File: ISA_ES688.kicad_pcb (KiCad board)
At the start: 4 copper layers, 104.1 x 99.1 mm, 114 parts, among them J1 ISA BUS, J2 Interrupt Select, J3 Address Select, J4 DMA Select, J5 Joystick/MIDI, J6 LINE OUT, J7 MIC, J8 LINE IN, J9 SPKR OUT, U1 74LS14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

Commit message: Add OPL logo
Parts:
- added G***: LOGO, ES688_ISA8:opl_logo, F.Cu at (279.9, 140.5)
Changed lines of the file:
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@@
     (tracks 2242)
     (zones 0)
-    (modules 114)
+    (modules 115)
     (nets 141)
   )
@@
     (add_net GNDA)
   )
+  (module ES688_ISA8:opl_logo (layer F.Cu)
+    (at 279.908 140.462)
+    (fp_text reference G*** (at 0 0) (layer F.SilkS) hide
+      (effects (font (size 1.524 1.524) (thickness 0.3)))
+    )
+    (fp_text value LOGO (at 0.75 0) (layer F.SilkS) hide
+      (effects (font (size 1.524 1.524) (thickness 0.3)))
+    )
+    (fp_poly (pts (xy -5.344685 -3.755461) (xy -5.028291 -3.532553) (xy -4.870695 -3.306566) (xy -4.785234 -3.06096)
+      (xy -4.836403 -2.880506) (xy -5.038005 -2.734348) (xy -5.148945 -2.684645) (xy -5.340285 -2.602747)
+      (xy -5.385019 -2.564591) (xy -5.293745 -2.550992) (xy -5.224318 -2.548228) (xy -4.929154 -2.46042)
+      (xy -4.69366 -2.238158) (xy -4.530761 -1.909744) (xy -4.453385 -1.503478) (xy -4.474458 -1.047663)
+      (xy -4.492892 -0.946891) (xy -4.735392 -0.17358) (xy -5.125128 0.575267) (xy -5.640015 1.277122)
+      (xy -6.257967 1.909459) (xy -6.9569 2.449749) (xy -7.714727 2.875466) (xy -8.509363 3.16408)
+      (xy -8.527992 3.168951) (xy -8.915534 3.257863) (xy -9.212041 3.28867) (xy -9.485398 3.261724)
+      (xy -9.803493 3.177379) (xy -9.809211 3.175598) (xy -10.27074 2.946837) (xy -10.64008 2.586699)
+      (xy -10.904681 2.113241) (xy -10.991105 1.779589) (xy -9.986381 1.779589) (xy -9.931695 2.127449)
+      (xy -9.858866 2.267161) (xy -9.660316 2.419537) (xy -9.361963 2.447399) (xy -8.959009 2.350373)
+      (xy -8.517884 2.16324) (xy -7.777485 1.721081) (xy -7.078147 1.145927) (xy -6.456397 0.474058)
+      (xy -5.948764 -0.258248) (xy -5.795526 -0.540542) (xy -5.625997 -0.935733) (xy -5.523953 -1.295382)
+      (xy -5.492475 -1.590942) (xy -5.534641 -1.793864) (xy -5.6515 -1.875435) (xy -6.136229 -1.846969)
+      (xy -6.695017 -1.693987) (xy -7.301904 -1.428612) (xy -7.930931 -1.062966) (xy -8.556139 -0.609172)
+      (xy -8.79995 -0.405155) (xy -9.194592 -0.002926) (xy -9.521744 0.444896) (xy -9.770218 0.910078)
+      (xy -9.928826 1.364387) (xy -9.986381 1.779589) (xy -10.991105 1.779589) (xy -11.051994 1.544523)
+      (xy -11.071343 1.359395) (xy -11.037587 0.657076) (xy -10.837736 -0.038683) (xy -10.475021 -0.72296)
+      (xy -9.952673 -1.390831) (xy -9.273923 -2.037374) (xy -8.442001 -2.657664) (xy -8.429934 -2.665705)
+      (xy -7.982337 -2.940247) (xy -7.490359 -3.203266) (xy -6.989666 -3.439293) (xy -6.515922 -3.632857)
+      (xy -6.104792 -3.768486) (xy -5.791941 -3.83071) (xy -5.738926 -3.833013) (xy -5.344685 -3.755461)) (layer F.SilkS) (width 0.01))
+    (fp_poly (pts (xy 0.503216 -3.833673) (xy 1.041462 -3.79121) (xy 1.478677 -3.711661) (xy 1.848138 -3.588639)
+      (xy 2.183117 -3.415761) (xy 2.233753 -3.384306) (xy 2.532571 -3.162193) (xy 2.733427 -2.918503)
+      (xy 2.853094 -2.61487) (xy 2.908349 -2.212928) (xy 2.917597 -1.820333) (xy 2.907511 -1.412893)
+      (xy 2.875215 -1.120056) (xy 2.811183 -0.887569) (xy 2.718102 -0.684242) (xy 2.362164 -0.171137)
+      (xy 1.871179 0.295316) (xy 1.277327 0.6951) (xy 0.612788 1.008196) (xy -0.090259 1.214587)
+      (xy -0.421112 1.26859) (xy -0.871948 1.311872) (xy -1.370258 1.343292) (xy -1.80978 1.356183)
+      (xy -1.818112 1.356208) (xy -2.497667 1.35775) (xy -2.921 2.084592) (xy -3.259968 2.611556)
+      (xy -3.568713 2.977675) (xy -3.845679 3.181926) (xy -4.089313 3.223283) (xy -4.29806 3.100724)
+      (xy -4.355533 3.029161) (xy -4.449987 2.854031) (xy -4.472924 2.670727) (xy -4.417048 2.445085)
+      (xy -4.275062 2.142937) (xy -4.099923 1.832313) (xy -3.91802 1.514983) (xy -3.814334 1.307527)
+      (xy -3.778129 1.175737) (xy -3.798667 1.0854) (xy -3.845923 1.023083) (xy -3.937024 0.839818)
+      (xy -3.979014 0.592448) (xy -3.979333 0.570978) (xy -3.904121 0.265069) (xy -3.79781 0.156237)
+      (xy -1.719497 0.156237) (xy -1.612922 0.238973) (xy -1.370759 0.290498) (xy -1.024672 0.306059)
+      (xy -0.785444 0.296504) (xy -0.280216 0.212722) (xy 0.278712 0.035556) (xy 0.387038 -0.007965)
+      (xy 1.005987 -0.306772) (xy 1.482386 -0.63448) (xy 1.842784 -1.011098) (xy 1.976732 -1.205965)
+      (xy 2.143766 -1.539879) (xy 2.17021 -1.79664) (xy 2.050468 -2.001327) (xy 1.778941 -2.179017)
+      (xy 1.757155 -2.18963) (xy 1.333872 -2.356314) (xy 0.89357 -2.468623) (xy 0.496218 -2.514)
+      (xy 0.277307 -2.49951) (xy 0.168494 -2.465977) (xy 0.057079 -2.394658) (xy -0.073779 -2.266019)
+      (xy -0.240923 -2.060526) (xy -0.461193 -1.758646) (xy -0.751432 -1.340845) (xy -0.865693 -1.173828)
+      (xy -1.141812 -0.765139) (xy -1.380016 -0.404645) (xy -1.5655 -0.115412) (xy -1.683456 0.079497)
+      (xy -1.719497 0.156237) (xy -3.79781 0.156237) (xy -3.682503 0.038197) (xy -3.320511 -0.104335)
+      (xy -3.181404 -0.130465) (xy -3.043805 -0.155523) (xy -2.928346 -0.198082) (xy -2.815014 -0.279107)
+      (xy -2.683794 -0.419561) (xy -2.51467 -0.640409) (xy -2.287629 -0.962614) (xy -2.033471 -1.33284)
+      (xy -1.248217 -2.480827) (xy -1.745942 -2.434846) (xy -2.116111 -2.376256) (xy -2.52533 -2.275935)
+      (xy -2.751667 -2.203094) (xy -3.070246 -2.095598) (xy -3.368429 -2.009851) (xy -3.534833 -1.973065)
+      (xy -3.725644 -1.958874) (xy -3.800654 -2.013857) (xy -3.809186 -2.086237) (xy -3.758052 -2.226327)
+      (xy -3.625226 -2.453409) (xy -3.440283 -2.726831) (xy -3.232801 -3.005941) (xy -3.032354 -3.250087)
+      (xy -2.868521 -3.418615) (xy -2.807637 -3.46286) (xy -2.491422 -3.58177) (xy -2.04196 -3.684618)
+      (xy -1.494987 -3.766221) (xy -0.88624 -3.821397) (xy -0.251456 -3.844964) (xy -0.169333 -3.845435)
+      (xy 0.503216 -3.833673)) (layer F.SilkS) (width 0.01))
+    (fp_poly (pts (xy 6.792524 -3.750129) (xy 6.968282 -3.621872) (xy 7.027333 -3.453164) (xy 6.982386 -3.323082)
+      (xy 6.858223 -3.081252) (xy 6.670866 -2.755941) (xy 6.436334 -2.375415) (xy 6.273265 -2.122643)
+      (xy 5.937648 -1.604888) (xy 5.558663 -1.010002) (xy 5.179524 -0.406375) (xy 4.843445 0.137599)
+      (xy 4.798297 0.211667) (xy 4.077398 1.397) (xy 4.430532 1.453363) (xy 4.671015 1.487661)
+      (xy 5.021594 1.532665) (xy 5.423994 1.581027) (xy 5.630333 1.604612) (xy 6.233483 1.684084)
+      (xy 6.758622 1.776651) (xy 7.185292 1.877139) (xy 7.493035 1.980378) (xy 7.661392 2.081196)
+      (xy 7.686221 2.124361) (xy 7.644179 2.248616) (xy 7.509438 2.449922) (xy 7.310177 2.686746)
+      (xy 7.289679 2.70877) (xy 6.867463 3.158486) (xy 6.164232 3.102333) (xy 5.722562 3.063039)
+      (xy 5.241381 3.014062) (xy 4.826 2.966141) (xy 4.190005 2.905187) (xy 3.550565 2.878429)
+      (xy 2.944805 2.884863) (xy 2.409851 2.923485) (xy 1.98283 2.99329) (xy 1.798258 3.048043)
+      (xy 1.457049 3.166205) (xy 1.23689 3.208893) (xy 1.10809 3.17777) (xy 1.046545 3.090144)
+      (xy 1.029114 2.871373) (xy 1.131844 2.593413) (xy 1.362268 2.237436) (xy 1.416402 2.165557)
+      (xy 1.673378 1.876669) (xy 1.936897 1.696224) (xy 2.139321 1.614499) (xy 2.247521 1.576507)
+      (xy 2.344585 1.531112) (xy 2.441818 1.463876) (xy 2.550531 1.360364) (xy 2.682031 1.206141)
+      (xy 2.847627 0.98677) (xy 3.058627 0.687817) (xy 3.32634 0.294844) (xy 3.662073 -0.206584)
+      (xy 4.077134 -0.830903) (xy 4.200495 -1.016725) (xy 4.592092 -1.603086) (xy 4.961021 -2.148745)
+      (xy 5.295287 -2.636475) (xy 5.582899 -3.049049) (xy 5.811863 -3.369238) (xy 5.970187 -3.579815)
+      (xy 6.040507 -3.659951) (xy 6.280583 -3.779238) (xy 6.547273 -3.805941) (xy 6.792524 -3.750129)) (layer F.SilkS) (width 0.01))
+    (fp_poly (pts (xy 9.153934 -3.630036) (xy 9.394952 -3.60197) (xy 9.519474 -3.562208) (xy 9.525 -3.556)
+      (xy 9.48923 -3.498388) (xy 9.316743 -3.471958) (xy 9.275997 -3.471333) (xy 8.974667 -3.471333)
+      (xy 8.974667 -2.751667) (xy 8.969244 -2.391872) (xy 8.949508 -2.171664) (xy 8.91025 -2.061543)
+      (xy 8.847667 -2.032) (xy 8.784173 -2.062725) (xy 8.745313 -2.174567) (xy 8.72588 -2.397027)
+      (xy 8.720667 -2.751667) (xy 8.720667 -3.471333) (xy 8.466667 -3.471333) (xy 8.288325 -3.495858)
+      (xy 8.212686 -3.554947) (xy 8.212667 -3.556) (xy 8.291405 -3.59875) (xy 8.504313 -3.628518)
+      (xy 8.816428 -3.640604) (xy 8.84267 -3.640667) (xy 9.153934 -3.630036)) (layer F.SilkS) (width 0.01))
+    (fp_poly (pts (xy 9.927514 -3.58917) (xy 10.04666 -3.418926) (xy 10.181623 -3.118589) (xy 10.390503 -2.596511)
+      (xy 10.55705 -3.097422) (xy 10.670946 -3.395463) (xy 10.777338 -3.559898) (xy 10.898221 -3.623865)
+      (xy 10.907465 -3.625389) (xy 10.992412 -3.629646) (xy 11.046124 -3.591831) (xy 11.075746 -3.481508)
+      (xy 11.088424 -3.268238) (xy 11.091304 -2.921587) (xy 11.091333 -2.842222) (xy 11.086839 -2.457202)
+      (xy 11.0704 -2.213038) (xy 11.037577 -2.081418) (xy 10.983932 -2.03403) (xy 10.964333 -2.032)
+      (xy 10.893792 -2.06865) (xy 10.853097 -2.1993) (xy 10.835091 -2.455007) (xy 10.832603 -2.6035)
+      (xy 10.827872 -3.175) (xy 10.673454 -2.794) (xy 10.52987 -2.521995) (xy 10.387411 -2.414657)
+      (xy 10.36774 -2.413) (xy 10.2341 -2.489213) (xy 10.108379 -2.723857) (xy 10.082389 -2.794)
+      (xy 9.948333 -3.175) (xy 9.923298 -2.6035) (xy 9.899523 -2.281268) (xy 9.858687 -2.100609)
+      (xy 9.793667 -2.034057) (xy 9.775131 -2.032) (xy 9.716092 -2.063684) (xy 9.678723 -2.177111)
+      (xy 9.658807 -2.399846) (xy 9.652124 -2.759452) (xy 9.652 -2.836333) (xy 9.654859 -3.21099)
+      (xy 9.667581 -3.447542) (xy 9.696385 -3.577178) (xy 9.747491 -3.631087) (xy 9.812371 -3.640667)
+      (xy 9.927514 -3.58917)) (layer F.SilkS) (width 0.01))
+  )
   (module ES688_ISA8:SOP-16 (layer F.Cu)

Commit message: Change silkscreen
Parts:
- moved G*** 2.36 mm to (281.3, 142.4)
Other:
- board text added: "INSIDE"

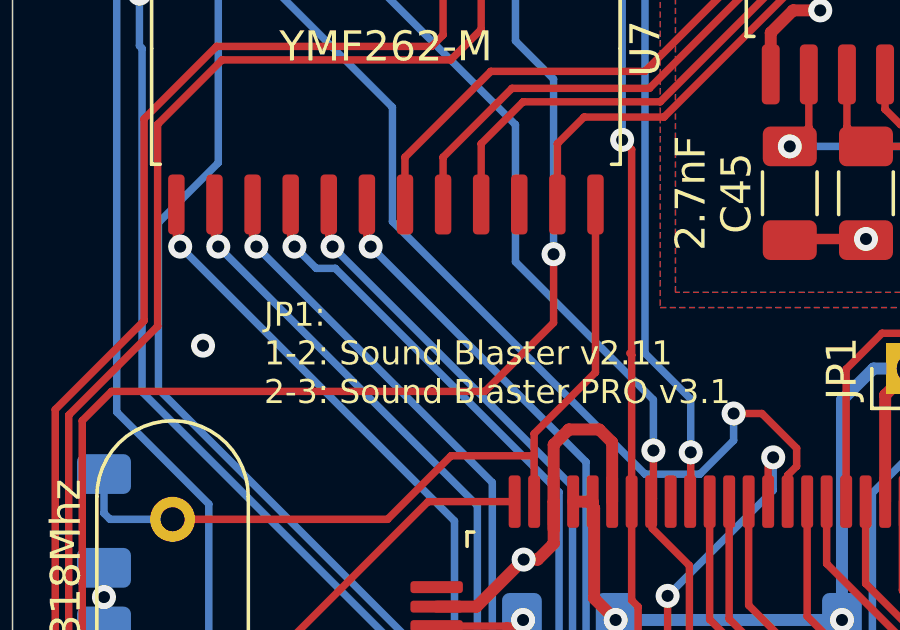
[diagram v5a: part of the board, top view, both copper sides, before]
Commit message: Further silkscreen changes
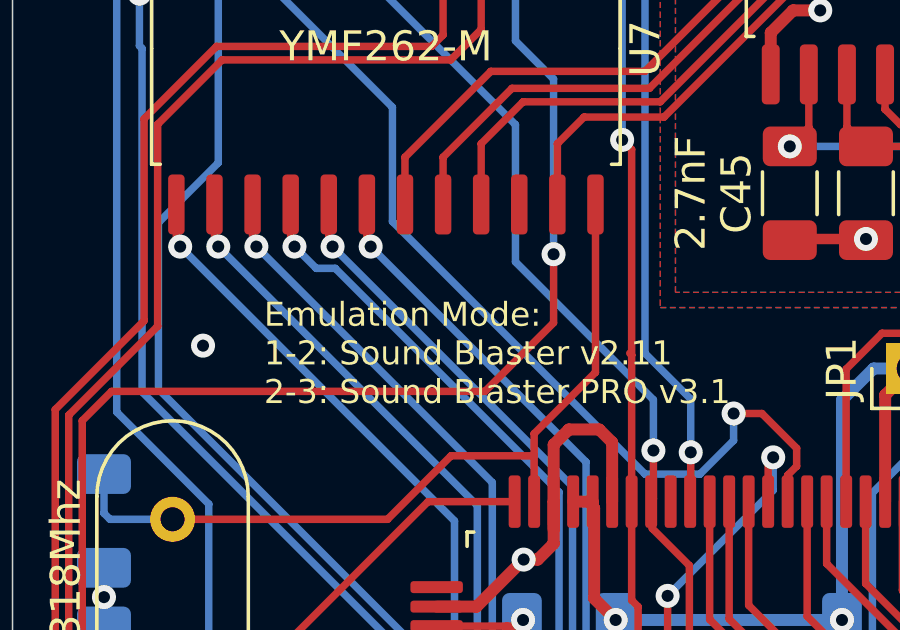
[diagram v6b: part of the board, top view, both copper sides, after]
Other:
- board text added: "Emulation Mode: 1-2: Sound Blaster v2.11 2-3: Sound Blaster PRO v3.1"
- board text removed: "JP1: 1-2: Sound Blaster v2.11 2-3: Sound Blaster PRO v3.1"
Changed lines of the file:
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@@
     (effects (font (size 1.5 1.5) (thickness 0.3)))
   )
-  (gr_text "JP1:\n1-2: Sound Blaster v2.11\n2-3: Sound Blaster PRO v3.1" (at 219.202 134.366) (layer F.SilkS)
+  (gr_text "Emulation Mode:\n1-2: Sound Blaster v2.11\n2-3: Sound Blaster PRO v3.1" (at 219.202 134.366) (layer F.SilkS)
     (effects (font (size 0.8 0.8) (thickness 0.15)) (justify left))
   )

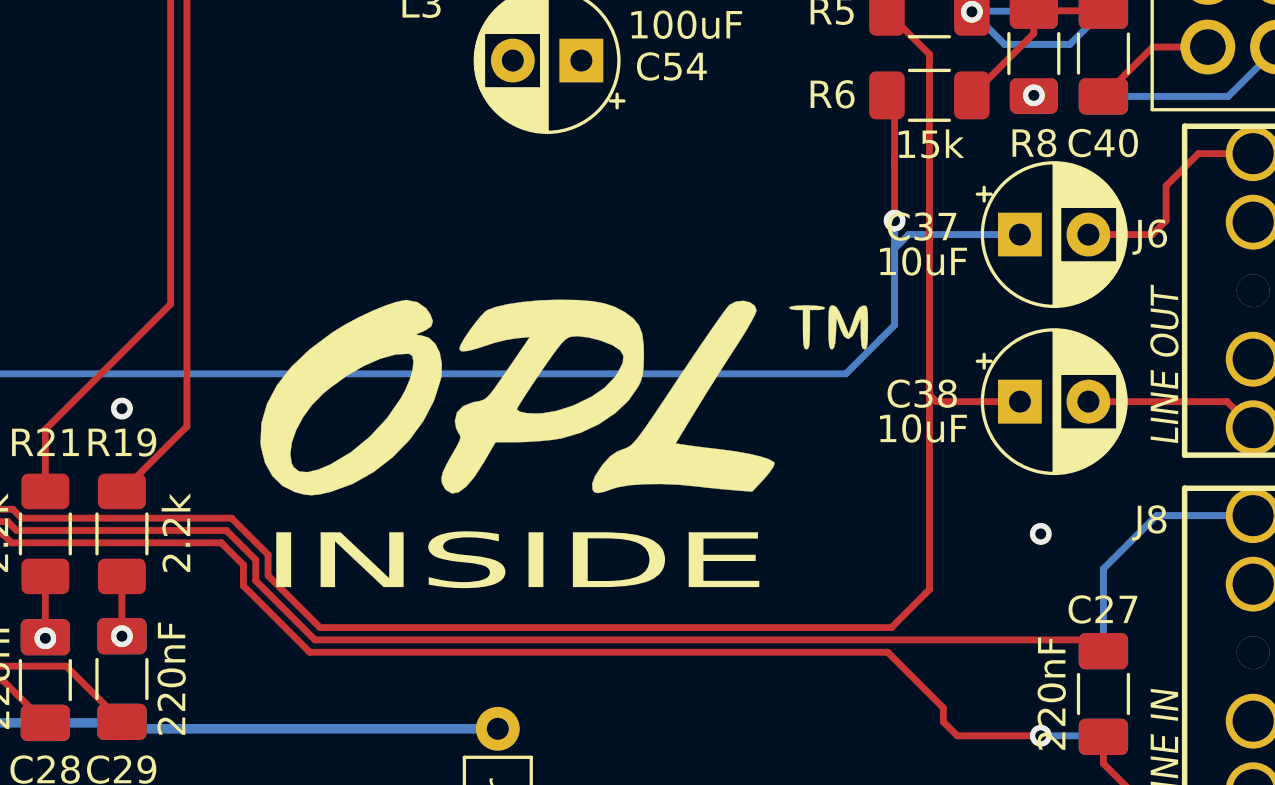
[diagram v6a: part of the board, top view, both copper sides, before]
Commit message: More silkscreen adjustments
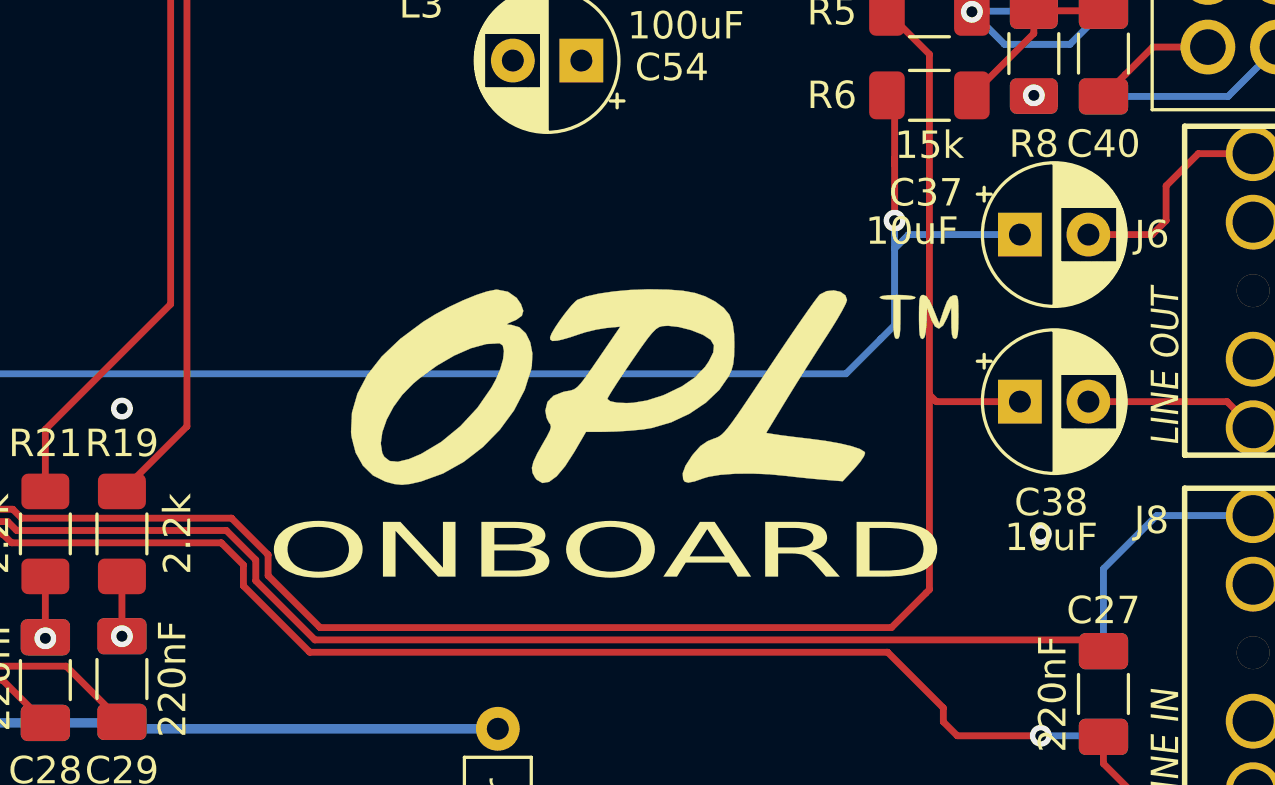
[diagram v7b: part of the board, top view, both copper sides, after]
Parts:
- moved G*** 3.32 mm to (284.6, 142.0)
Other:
- board text added: "ONBOARD"
- board text removed: "INSIDE"
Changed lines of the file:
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@@
   )
   (module ES688_ISA8:opl_logo (layer F.Cu)
-    (at 281.305 142.367)
+    (at 284.607 141.986)
     (fp_text reference G*** (at 0 0) (layer F.SilkS) hide
       (effects (font (size 1.524 1.524) (thickness 0.3)))
@@
     (descr "CP, Radial series, Radial, pin pitch=2.50mm, , diameter=5mm, Electrolytic Capacitor")
     (tags "CP Radial series Radial pin pitch 2.50mm  diameter 5mm Electrolytic Capacitor")
-    (fp_text reference C38 (at -3.556 -0.254) (layer F.SilkS)
+    (fp_text reference C38 (at 1.143 3.683) (layer F.SilkS)
       (effects (font (size 1 1) (thickness 0.15)))
     )
-    (fp_text value 10uF (at -3.556 1.016) (layer F.SilkS)
+    (fp_text value 10uF (at 1.143 4.953) (layer F.SilkS)
       (effects (font (size 1 1) (thickness 0.15)))
     )
@@
     (descr "CP, Radial series, Radial, pin pitch=2.50mm, , diameter=5mm, Electrolytic Capacitor")
     (tags "CP Radial series Radial pin pitch 2.50mm  diameter 5mm Electrolytic Capacitor")
-    (fp_text reference C37 (at -3.556 -0.254) (layer F.SilkS)
+    (fp_text reference C37 (at -3.429 -1.524) (layer F.SilkS)
       (effects (font (size 1 1) (thickness 0.15)))
     )
-    (fp_text value 10uF (at -3.556 1.016) (layer F.SilkS)
+    (fp_text value 10uF (at -3.937 -0.127) (layer F.SilkS)
       (effects (font (size 1 1) (thickness 0.15)))
     )
@@
     )
   )
-  (gr_text INSIDE (at 279.527 148.082) (layer F.SilkS)
-    (effects (font (size 2 4) (thickness 0.3)))
+  (gr_text ONBOARD (at 282.829 147.701) (layer F.SilkS)
+    (effects (font (size 2 3.5) (thickness 0.3)))
   )
   (gr_line (start 235.458 176.846) (end 237.998 176.846) (layer F.SilkS) (width 0.12))
